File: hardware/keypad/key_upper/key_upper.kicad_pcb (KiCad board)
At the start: 2 copper layers, 18 x 76.2 mm, 23 parts, among them J1 Hub (JST-GH 8), SW1 Kailh Box Navy, SW2 Kailh Box Navy, SW3 Kailh Box Navy, U1 TCA9534APWR

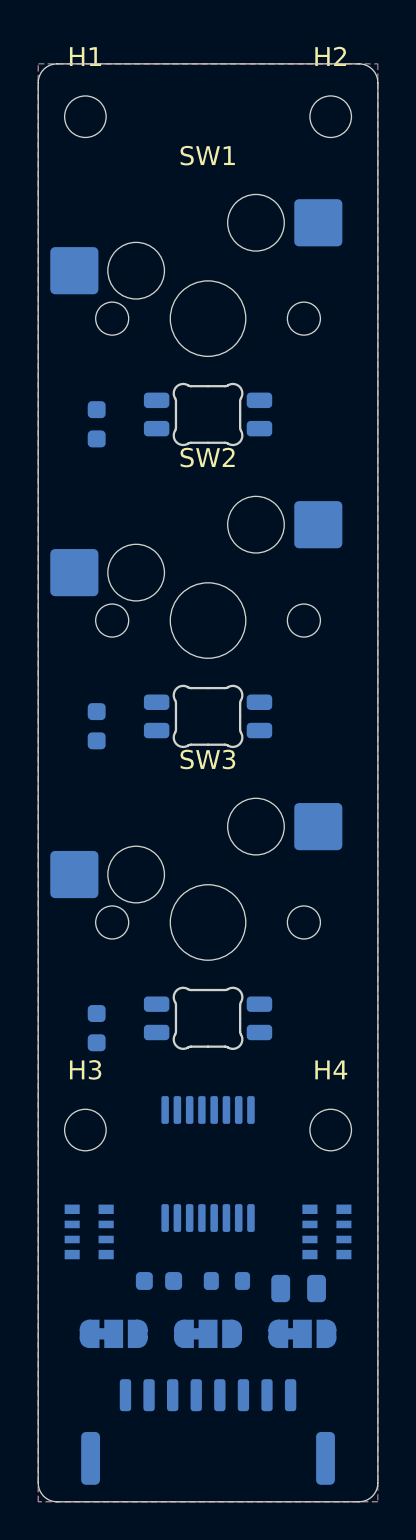
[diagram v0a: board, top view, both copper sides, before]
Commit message: Upper keypad board laid out and routed
The user's layout and routing, with review fixes: the KEY1 hop via moved
clear of KEY2 and KEY5, stray stubs removed, J1's ground pin given its own
via, +3V3 necked past the SDA pin, and the silkscreen tidied. DRC is clean
apart from the hotswap socket outlines over their holes. The LED window is
opposite the switch's metal pins, which matches the footprints.

Co-Authored-By: Claude Opus 5.5 <noreply@anthropic.com>
Claude-Session: https://claude.ai/code/session_01UUhpevE9ZSCJvyu3edQmf9
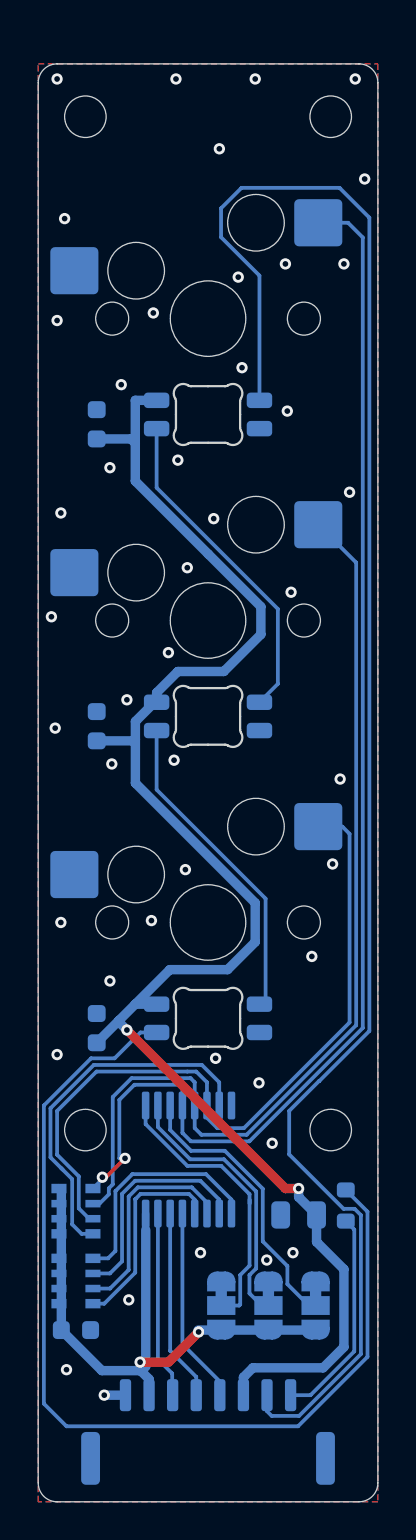
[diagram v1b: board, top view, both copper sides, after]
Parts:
- moved RN2 13.6 mm to (93.0, 124.5), turned to 180 degrees
- moved R1 7.46 mm to (107.3, 120.5), turned to -90 degrees
- moved JP1 5.89 mm to (100.7, 125.8), turned to -90 degrees
- moved C1 5.11 mm to (93.0, 127.1)
- moved C2 3.90 mm to (104.8, 121.0), turned to 180 degrees
- moved JP2 3.53 mm to (103.2, 125.8), turned to -90 degrees
- moved JP3 1.66 mm to (105.7, 125.8), turned to -90 degrees
- moved RN1 1.30 mm to (93.0, 120.8), turned to 180 degrees
- moved U1 1.06 mm to (99.0, 118.1), turned to -90 degrees
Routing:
- net LED_DIN: track 0.00 -> 91.2 mm
- net +5V: track 0.00 -> 85.0 mm, vias 0 -> 2
- net KEY1: track 0.00 -> 68.2 mm, vias 0 -> 2
- net LED_LAST: track 0.00 -> 51.9 mm
- net KEY2: track 0.00 -> 51.5 mm
- net KEY3: track 0.00 -> 38.3 mm
- net +3V3: track 0.00 -> 33.0 mm, vias 0 -> 2
- net KEY4: track 0.00 -> 19.1 mm
- net LED1: track 0.00 -> 17.6 mm
- net LED2: track 0.00 -> 17.0 mm
- net ADDR0: track 0.00 -> 15.3 mm
- net ADDR2: track 0.00 -> 15.1 mm
- net ADDR1: track 0.00 -> 14.6 mm
- net KEY5: track 0.00 -> 12.3 mm
- net KEY6: track 0.00 -> 12.0 mm
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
